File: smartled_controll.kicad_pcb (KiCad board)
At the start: 2 copper layers, 68 parts, among them J1 Conn_01x04, SW1 SW_Push, U1 OC5028B, U2 MAX485E, U3 PY32F003F1xUx, U4 OC5864, U5 need chooice, U7 need chooice, Y1 Crystal_GND23

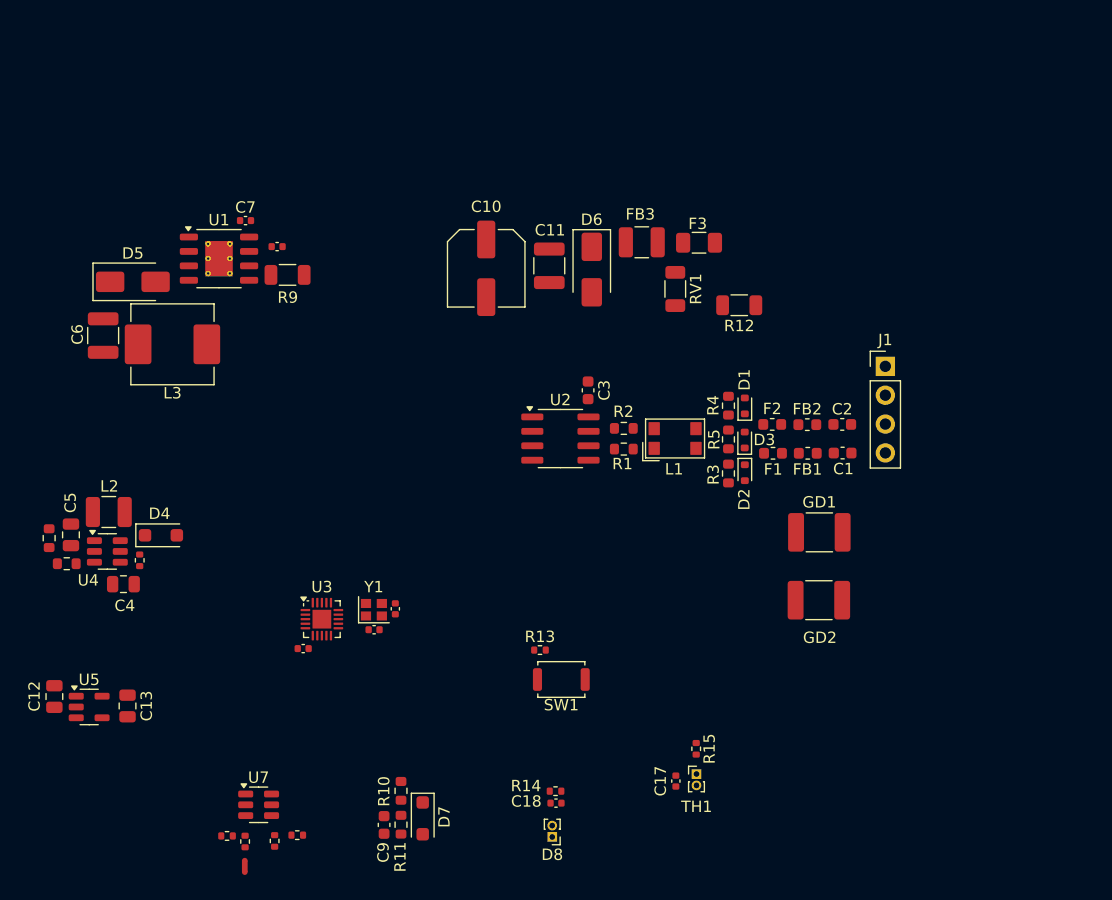
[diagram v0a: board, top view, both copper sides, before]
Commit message: 布线和调整布局，把PCB上的电路按模块分组
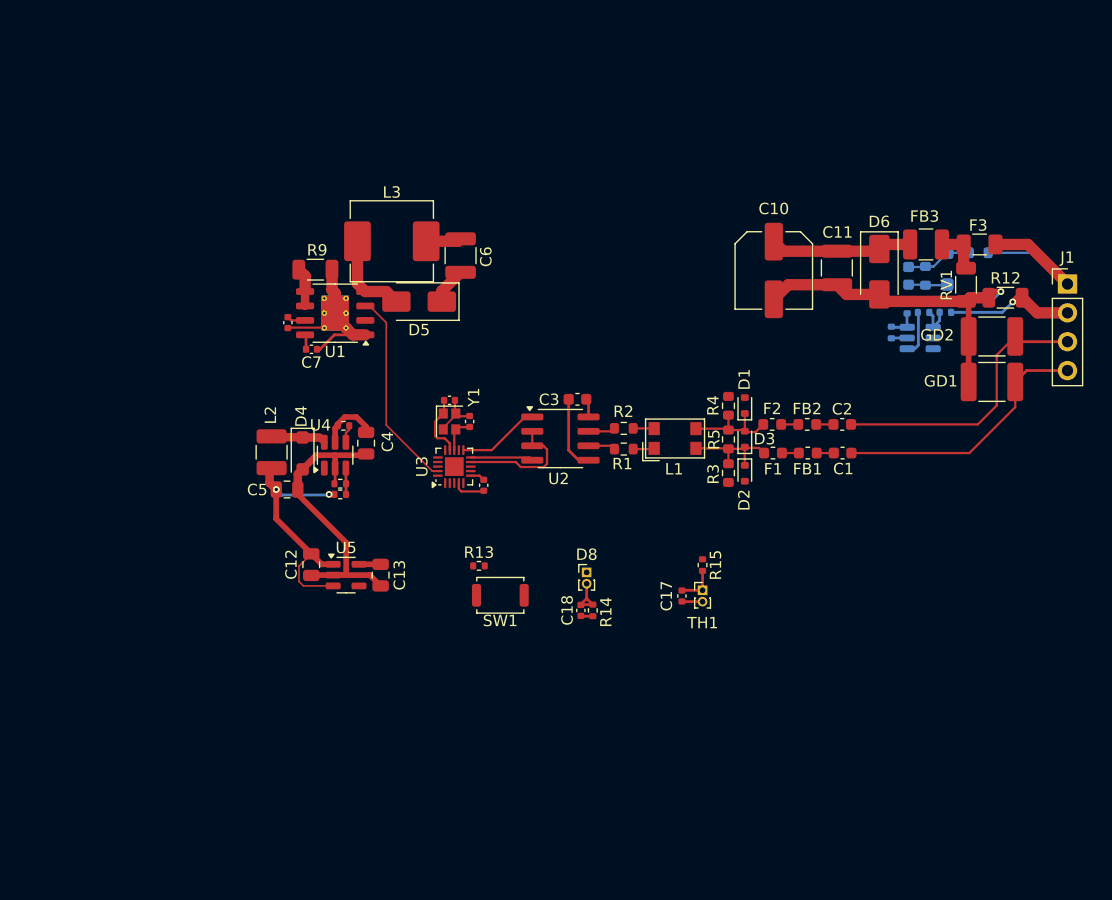
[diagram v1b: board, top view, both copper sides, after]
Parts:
- C9, D7, R10, R11, R16, R17, R18, R19, U7: moved to B.Cu
- R6, R7: footprint Resistor_SMD:R_0603_1608Metric -> Resistor_SMD:R_0402_1005Metric
- moved NT1 83.2 mm to (185.4, 75.6), turned to 0 degrees
- moved R17 75.2 mm to (181.0, 77.5), turned to 180 degrees
- moved R16 74.9 mm to (177.6, 77.0), turned to -90 degrees
- moved R19 73.4 mm to (176.2, 79.2), turned to -90 degrees
- moved R18 71.8 mm to (179.1, 77.5), turned to 0 degrees
- moved U7 71.3 mm to (178.8, 79.7)
- moved R10 69.5 mm to (183.9, 72.2), turned to 180 degrees
- moved D7 66.9 mm to (181.2, 73.6)
- moved C9 66.8 mm to (177.8, 74.2)
- moved R11 66.8 mm to (179.2, 74.2)
- moved C6 32.2 mm to (138.3, 72.5), turned to 90 degrees
- moved GD2 27.8 mm to (185.1, 79.6), turned to 180 degrees
- moved R6 25.9 mm to (127.7, 93.5), turned to 180 degrees
- moved RV1 25.6 mm to (182.8, 75.0)
- moved C12 25.4 mm to (125.2, 99.7)
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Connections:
- GD1 pad 1: GND -> /485+
- GD1 pad 2: (no net) -> GND
- GD2 pad 1: GND -> /485-
- GD2 pad 2: (no net) -> GND
- U3 pad 16: unconnected-(U3-PA0-Pad16) -> /PWM3
- U3 pad 17: unconnected-(U3-PA1-Pad17) -> /PWM4
- U3 pad 19: unconnected-(U3-PA3-Pad19) -> /PWM1
- U3 pad 7: unconnected-(U3-PA13_SWD-Pad7) -> /PWM2
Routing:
- net GND: track 0.00 -> 95.2 mm
- net +5V: track 0.00 -> 26.5 mm, vias 0 -> 2
- net /485-: track 0.00 -> 25.1 mm
- net /485+: track 0.00 -> 23.3 mm
- net VINP: track 0.00 -> 21.2 mm
- net /PWM1: track 0.00 -> 17.7 mm
- net /VIN+: track 0.00 -> 15.9 mm
- net /VIN-: track 0.00 -> 11.3 mm, vias 0 -> 1
- net /MAX485_TR: track 0.00 -> 11.0 mm
- net Net-(D2-K): track 0.00 -> 8.88 mm
- net Net-(D1-K): track 0.00 -> 8.82 mm
- net /Isamp+: track 0.00 -> 8.63 mm, vias 0 -> 1
- net Net-(D5-A): track 0.00 -> 7.81 mm
- net /MAX485_RO: track 0.00 -> 7.27 mm
- net /ADC_V: track 0.00 -> 5.87 mm
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
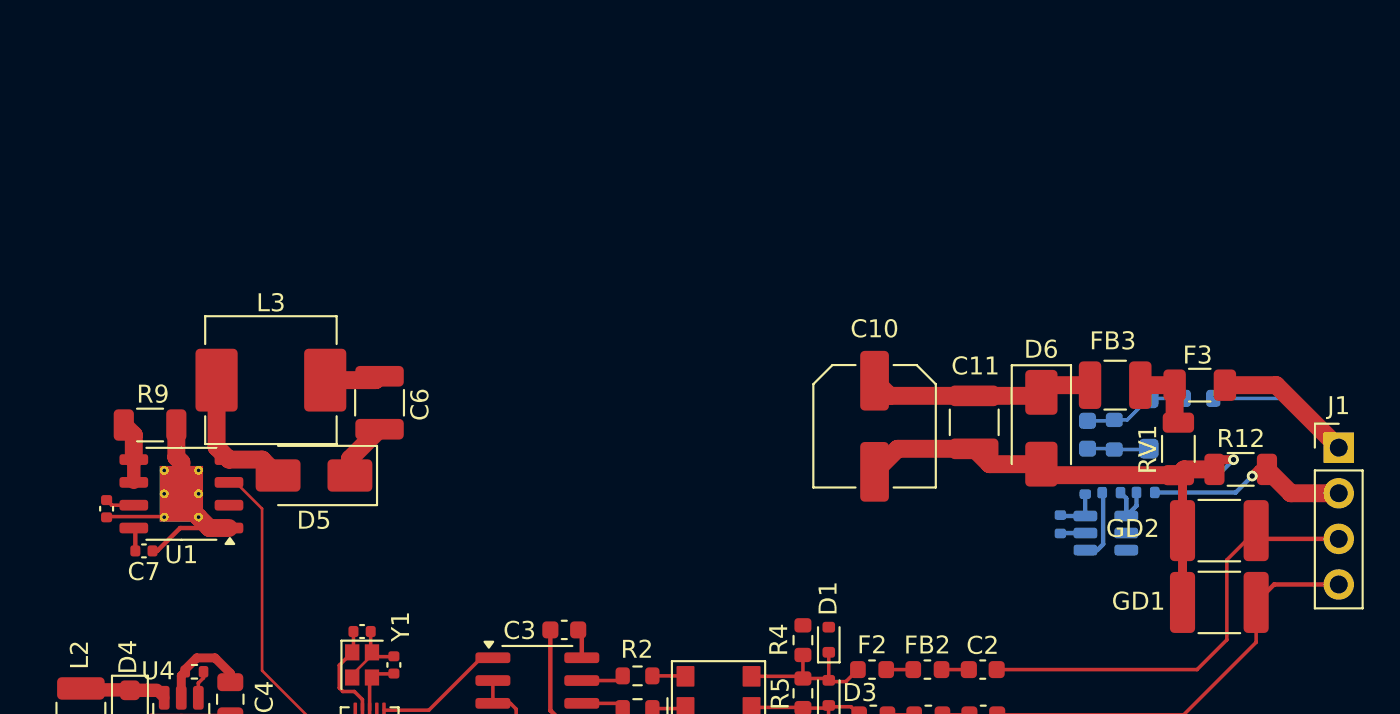
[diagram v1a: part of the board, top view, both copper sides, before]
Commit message: 复制LED驱动模块为4个
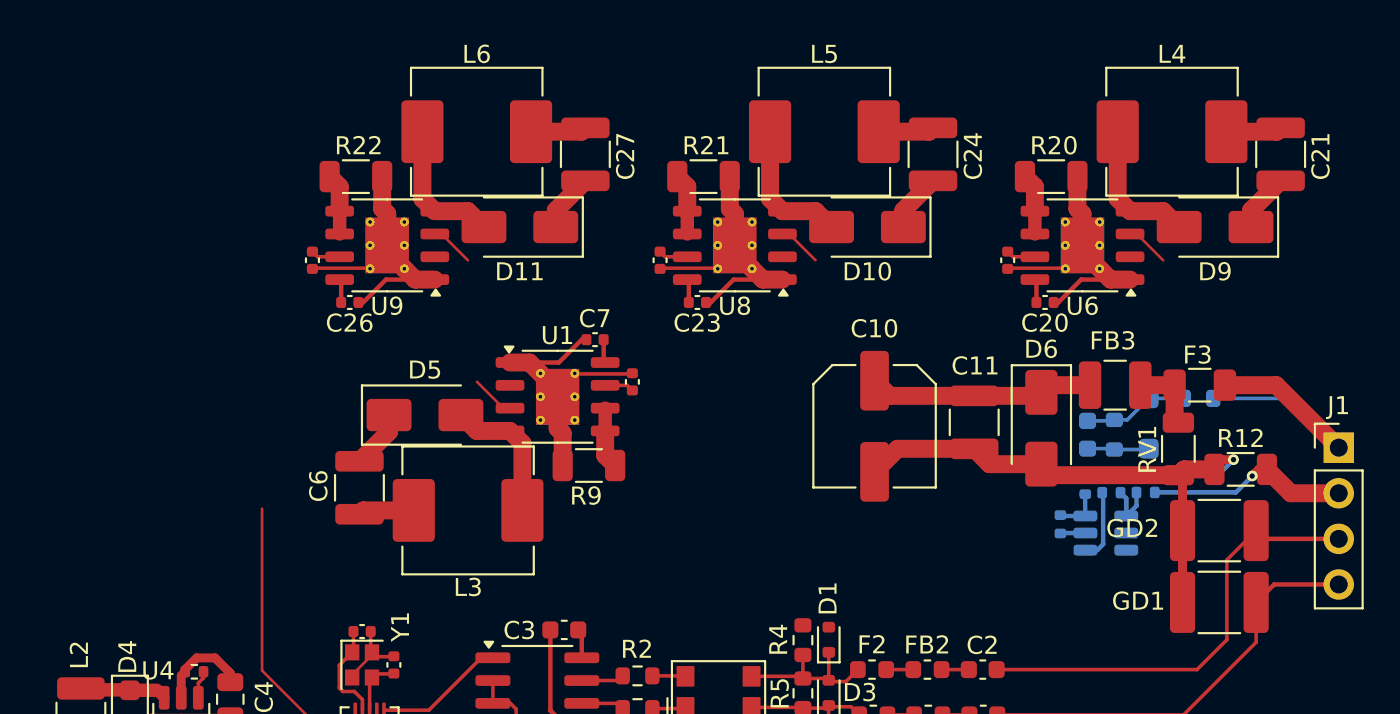
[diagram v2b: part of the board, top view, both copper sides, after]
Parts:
- added C19: C_Small, Capacitor_SMD:C_0402_1005Metric, F.Cu at (173.3, 64.5)
- added C20: C_Small, Capacitor_SMD:C_0402_1005Metric, F.Cu at (175.4, 66.9)
- added C21: C, Capacitor_SMD:C_1210_3225Metric, F.Cu at (188.5, 58.6)
- added C22: C_Small, Capacitor_SMD:C_0402_1005Metric, F.Cu at (153.9, 64.5)
- added C23: C_Small, Capacitor_SMD:C_0402_1005Metric, F.Cu at (156.0, 66.9)
- added C24: C, Capacitor_SMD:C_1210_3225Metric, F.Cu at (169.1, 58.6)
- added C25: C_Small, Capacitor_SMD:C_0402_1005Metric, F.Cu at (134.6, 64.5)
- added C26: C_Small, Capacitor_SMD:C_0402_1005Metric, F.Cu at (136.7, 66.9)
- added C27: C, Capacitor_SMD:C_1210_3225Metric, F.Cu at (149.8, 58.6)
- added D10: D_Schottky, Diode_SMD:D_SMA, F.Cu at (165.5, 62.7)
- added D11: D_Schottky, Diode_SMD:D_SMA, F.Cu at (146.1, 62.7)
- added D9: D_Schottky, Diode_SMD:D_SMA, F.Cu at (184.9, 62.7)
- added L4: L, Inductor_SMD:L_APV_APH0630, F.Cu at (182.5, 57.4)
- added L5: L, Inductor_SMD:L_APV_APH0630, F.Cu at (163.1, 57.4)
- added L6: L, Inductor_SMD:L_APV_APH0630, F.Cu at (143.7, 57.4)
- added R20: R, Resistor_SMD:R_1206_3216Metric, F.Cu at (175.7, 59.9)
- added R21: R, Resistor_SMD:R_1206_3216Metric, F.Cu at (156.4, 59.9)
- added R22: R, Resistor_SMD:R_1206_3216Metric, F.Cu at (137.0, 59.9)
- added U6: OC5028B, Package_SO:HSOP-8-1EP_3.9x4.9mm_P1.27mm_EP2.41x3.1mm_ThermalVias, F.Cu at (177.5, 63.7)
- added U8: OC5028B, Package_SO:HSOP-8-1EP_3.9x4.9mm_P1.27mm_EP2.41x3.1mm_ThermalVias, F.Cu at (158.1, 63.7)
- added U9: OC5028B, Package_SO:HSOP-8-1EP_3.9x4.9mm_P1.27mm_EP2.41x3.1mm_ThermalVias, F.Cu at (138.8, 63.7)
- moved C8 30.1 mm to (152.4, 71.3), turned to -90 degrees
- moved C7 27.7 mm to (150.3, 69.0), turned to 0 degrees
- moved R9 24.5 mm to (150.0, 76.0), turned to 180 degrees
- moved U1 21.6 mm to (148.2, 72.1), turned to 0 degrees
- moved L3 13.2 mm to (143.3, 78.5), turned to 180 degrees
- moved D5 7.04 mm to (140.9, 73.2), turned to 0 degrees
- moved C6 4.87 mm to (137.2, 77.2), turned to -90 degrees
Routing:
- net GND: track 95.2 -> 150.3 mm
- net VINP: track 21.2 -> 30.9 mm
- net Net-(D10-A): track 0.00 -> 7.81 mm
- net Net-(D9-A): track 0.00 -> 7.81 mm
- net Net-(D11-A): track 0.00 -> 7.81 mm
- net +5V: track 26.5 -> 30.4 mm
- net Net-(R22-Pad1): track 0.00 -> 3.43 mm
- net Net-(R21-Pad1): track 0.00 -> 3.43 mm
- net Net-(R20-Pad1): track 0.00 -> 3.43 mm
- net Net-(C27-Pad2): track 0.00 -> 3.11 mm
- net Net-(C24-Pad2): track 0.00 -> 3.11 mm
- net Net-(C21-Pad2): track 0.00 -> 3.11 mm
- net /PWM3: track 0.00 -> 2.45 mm
- net /PWM4: track 0.00 -> 2.45 mm
- net /PWM2: track 0.00 -> 2.45 mm
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
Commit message: 布线和微调布局（除光电二极管和温度传感器外）
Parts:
- moved C4 35.3 mm to (162.1, 74.4)
- moved L2 35.3 mm to (153.8, 75.2)
- moved R8 35.3 mm to (160.1, 72.8)
- moved C5 35.3 mm to (155.2, 78.4)
- moved D4 35.3 mm to (156.5, 75.3)
- moved R6 35.3 mm to (159.8, 78.9)
- moved R7 35.3 mm to (159.8, 77.9)
- moved U4 35.3 mm to (159.4, 75.4)
- moved C13 33.4 mm to (159.1, 82.2)
- moved C12 33.4 mm to (153.0, 81.3)
- moved U5 33.4 mm to (156.1, 82.2)
- moved SW1 17.0 mm to (141.3, 85.4), turned to 90 degrees
- moved R13 16.6 mm to (138.7, 83.2), turned to 180 degrees
- moved C17 3.45 mm to (154.8, 100.7)
- moved TH1 3.45 mm to (156.6, 100.2)
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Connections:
- U3 pad 16: /PWM3 -> /PWM1
- U3 pad 19: /PWM1 -> /PWM3
- U3 pad 2: unconnected-(U3-PA6-Pad2) -> /ADC_I
- U3 pad 3: unconnected-(U3-PA7-Pad3) -> /ADC_V
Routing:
- net GND: track 150.3 -> 272.6 mm, vias 0 -> 2
- net VINP: track 30.9 -> 105.6 mm
- net +5V: track 30.4 -> 95.5 mm, vias 2 -> 6
- net /PWM3: track 2.45 -> 60.7 mm, vias 0 -> 2
- net /PWM2: track 2.45 -> 57.2 mm, vias 0 -> 2
- net +3.3V: track 3.19 -> 55.3 mm, vias 0 -> 4
- net /ADC_V: track 5.87 -> 55.2 mm, vias 0 -> 1
- net /ADC_I: track 4.02 -> 51.2 mm, vias 0 -> 1
- net /PWM4: track 2.45 -> 38.8 mm, vias 0 -> 2
- net /PUSH: track 0.00 -> 10.4 mm
- net /PWM1: track 17.7 -> 27.8 mm, vias 0 -> 2

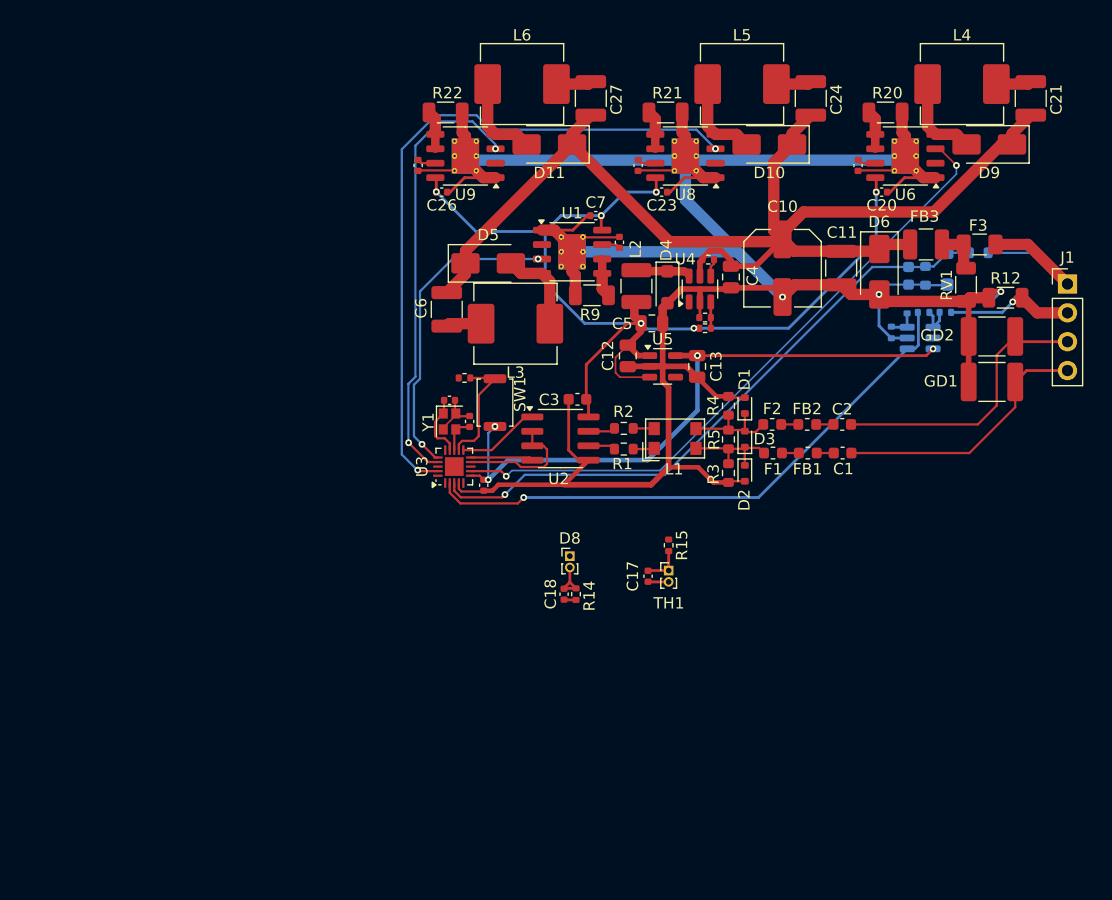
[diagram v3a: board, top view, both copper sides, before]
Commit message: 调整布局，划出PCB边框，MCU连接光电二极管和温度传感器
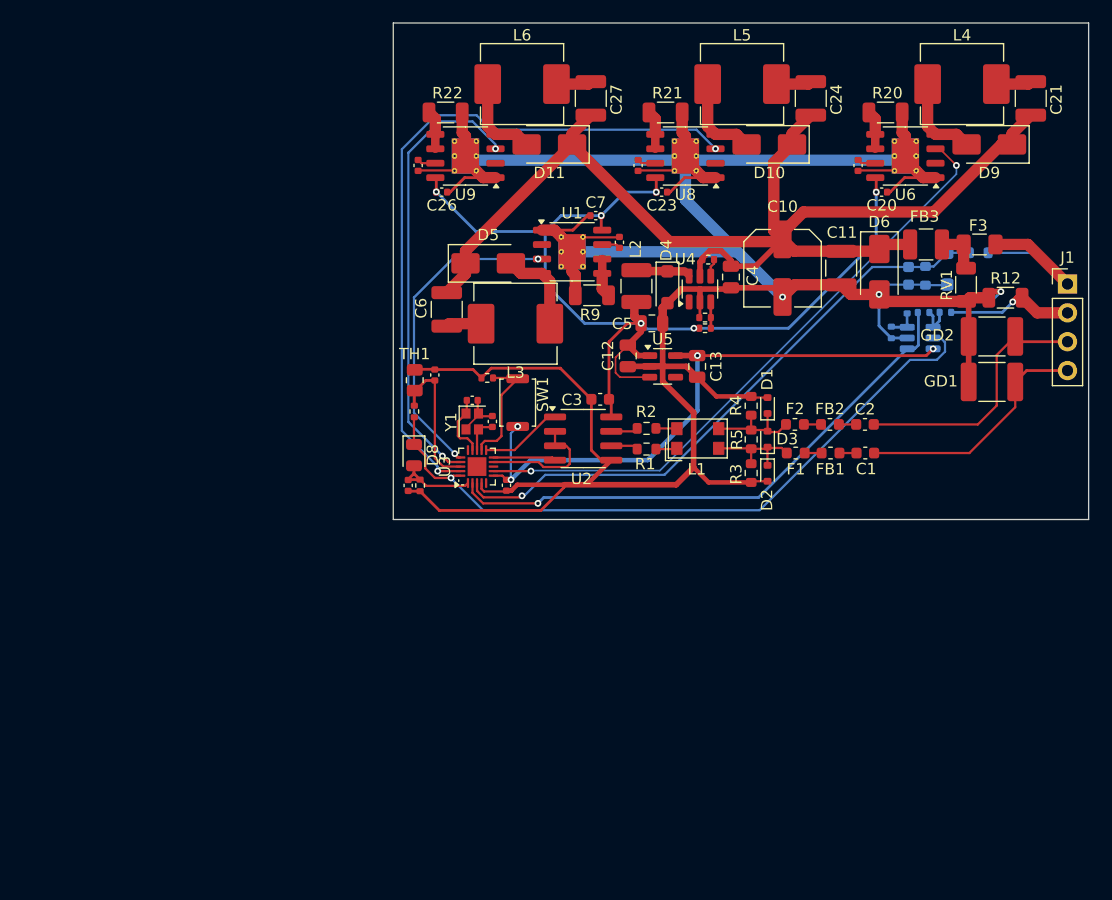
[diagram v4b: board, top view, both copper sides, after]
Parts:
- D8: footprint Connector_PinHeader_1.00mm:PinHeader_1x02_P1.00mm_Vertical -> Diode_SMD:D_0805_2012Metric
- TH1: footprint Connector_PinHeader_1.00mm:PinHeader_1x02_P1.00mm_Vertical -> Resistor_SMD:R_0805_2012Metric
- moved TH1 27.9 mm to (134.3, 83.4), turned to 90 degrees
- moved C17 25.8 mm to (136.1, 83.0), turned to 90 degrees
- moved R15 25.3 mm to (134.2, 86.2), turned to 90 degrees
- moved C18 16.7 mm to (133.7, 92.7)
- moved R14 16.7 mm to (134.8, 92.7)
- moved D8 16.3 mm to (134.2, 90.0), turned to -90 degrees
- moved C1 2.00 mm to (173.9, 89.8)
- moved C14 2.00 mm to (141.1, 87.1)
- moved C15 2.00 mm to (139.3, 85.2)
- moved C16 2.00 mm to (142.4, 92.7)
- moved C2 2.00 mm to (173.9, 87.3)
- moved C3 2.00 mm to (150.6, 85.1)
- moved D1 2.00 mm to (165.3, 85.7)
- moved D2 2.00 mm to (165.3, 91.6)
- moved D3 2.00 mm to (165.3, 88.6)
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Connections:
- U3 pad 1: unconnected-(U3-PA5-Pad1) -> /ADC_PD
- U3 pad 18: unconnected-(U3-PA2-Pad18) -> /ADC_T
- U3 pad 20: unconnected-(U3-PA4-Pad20) -> /SampEn
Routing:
- net /SampEn: track 0.00 -> 60.9 mm, vias 0 -> 1
- net GND: track 272.6 -> 305.5 mm
- net /ADC_T: track 3.53 -> 12.8 mm
- net /ADC_PD: track 3.91 -> 7.83 mm
- net /PWM2: track 57.2 -> 54.8 mm
- net /ADC_V: track 55.2 -> 53.2 mm
- net /ADC_I: track 51.2 -> 49.2 mm
- net /485+: track 23.3 -> 21.3 mm
- net /485-: track 25.1 -> 23.1 mm
- net +3.3V: track 55.3 -> 53.3 mm
- net /PWM3: track 60.7 -> 61.7 mm
- net /PWM4: track 38.8 -> 39.8 mm
- net +5V: track 95.5 -> 94.6 mm
- net /PWM1: track 27.8 -> 28.6 mm
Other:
- board outline added: 61.2 x 43.7 mm
